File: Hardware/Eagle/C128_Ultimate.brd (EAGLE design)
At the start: 62.2 x 83.2 mm, 5 parts, among them IC1 0RB_COMMODORE_EXPANSION_PORT_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, X4 TSW-122-07-G-Q

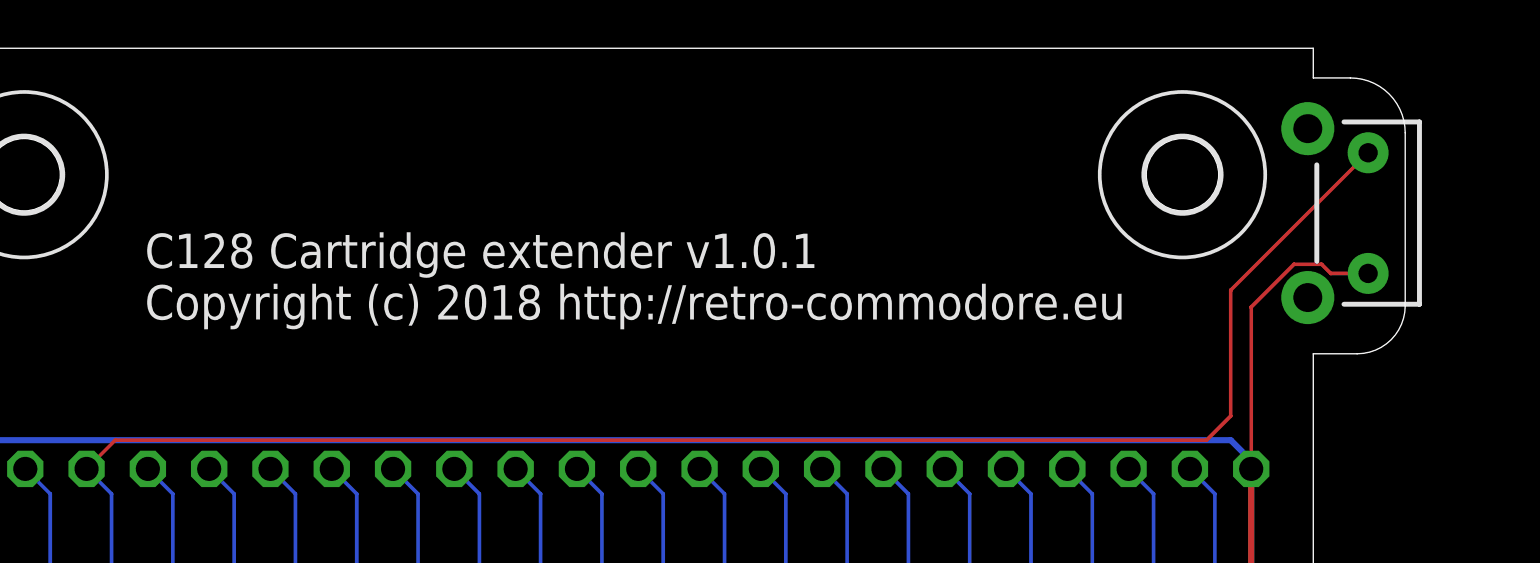
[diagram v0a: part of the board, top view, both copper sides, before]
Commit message: Update Hardware/Eagle/C128_Ultimate.brd
Properly moved reset button to bottom side
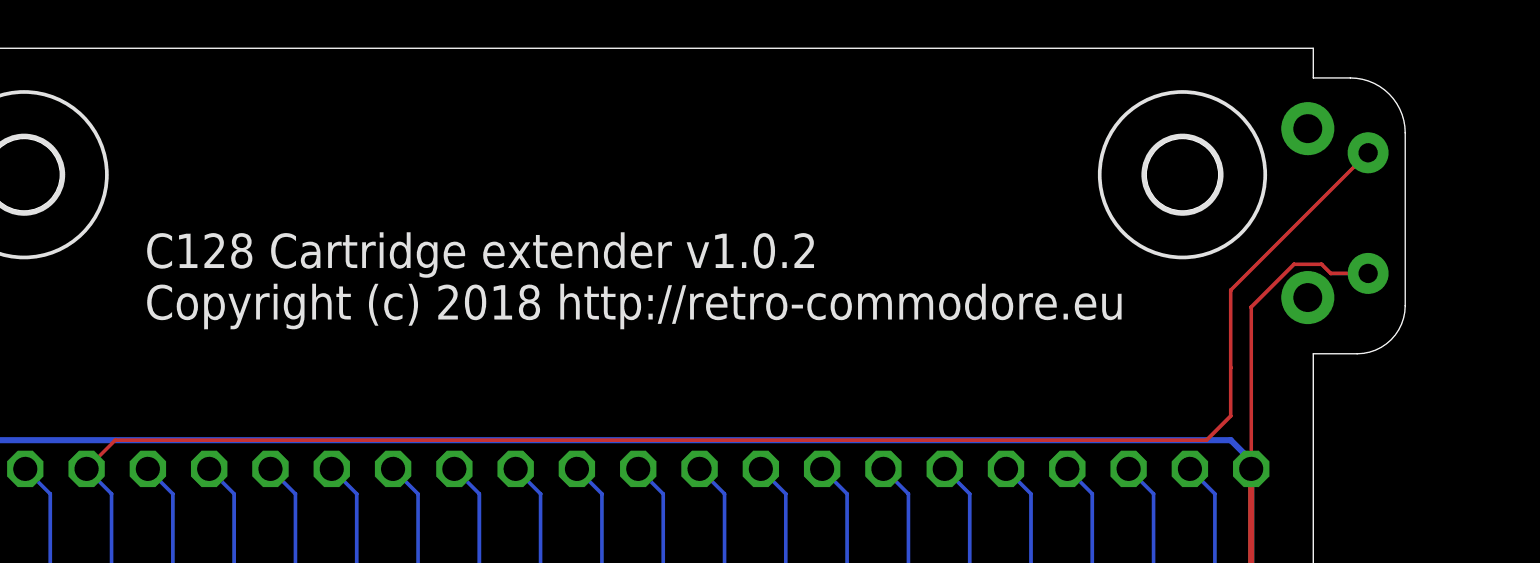
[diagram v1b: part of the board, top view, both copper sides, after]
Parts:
- flipped S1 to the bottom, turned to 270 degrees
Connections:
- net !RES: now also S1.1; no longer S1.2
- net GND: now also S1.2; no longer S1.1
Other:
- board text added: "C128 Cartridge extender v1.0.2 Copyright (c) 2018 http://retro-commodore.eu"
- board text removed: "C128 Cartridge extender v1.0.1 Copyright (c) 2018 http://retro-commodore.eu"
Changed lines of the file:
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@@
 <layers>
 <layer number="1" name="Top" color="4" fill="1" visible="yes" active="yes"/>
-<layer number="16" name="Bottom" color="1" fill="1" visible="yes" active="yes"/>
+<layer number="16" name="Bottom" color="1" fill="1" visible="no" active="yes"/>
 <layer number="17" name="Pads" color="2" fill="1" visible="yes" active="yes"/>
 <layer number="18" name="Vias" color="2" fill="1" visible="yes" active="yes"/>
@@
 <layer number="20" name="Dimension" color="24" fill="1" visible="yes" active="yes"/>
 <layer number="21" name="tPlace" color="7" fill="1" visible="yes" active="yes"/>
-<layer number="22" name="bPlace" color="7" fill="1" visible="yes" active="yes"/>
+<layer number="22" name="bPlace" color="7" fill="1" visible="no" active="yes"/>
 <layer number="23" name="tOrigins" color="15" fill="1" visible="yes" active="yes"/>
-<layer number="24" name="bOrigins" color="15" fill="1" visible="yes" active="yes"/>
+<layer number="24" name="bOrigins" color="15" fill="1" visible="no" active="yes"/>
 <layer number="25" name="tNames" color="7" fill="1" visible="yes" active="yes"/>
-<layer number="26" name="bNames" color="7" fill="1" visible="yes" active="yes"/>
+<layer number="26" name="bNames" color="7" fill="1" visible="no" active="yes"/>
 <layer number="27" name="tValues" color="7" fill="1" visible="no" active="yes"/>
 <layer number="28" name="bValues" color="7" fill="1" visible="no" active="yes"/>
@@
 <layer number="38" name="bTest" color="7" fill="1" visible="no" active="yes"/>
 <layer number="39" name="tKeepout" color="4" fill="11" visible="yes" active="yes"/>
-<layer number="40" name="bKeepout" color="1" fill="11" visible="yes" active="yes"/>
+<layer number="40" name="bKeepout" color="1" fill="11" visible="no" active="yes"/>
 <layer number="41" name="tRestrict" color="4" fill="10" visible="yes" active="yes"/>
-<layer number="42" name="bRestrict" color="1" fill="10" visible="yes" active="yes"/>
+<layer number="42" name="bRestrict" color="1" fill="10" visible="no" active="yes"/>
 <layer number="43" name="vRestrict" color="2" fill="10" visible="no" active="yes"/>
 <layer number="44" name="Drills" color="7" fill="1" visible="no" active="yes"/>
@@
 <layer number="50" name="dxf" color="7" fill="1" visible="no" active="no"/>
 <layer number="51" name="tDocu" color="7" fill="1" visible="yes" active="yes"/>
-<layer number="52" name="bDocu" color="7" fill="1" visible="yes" active="yes"/>
+<layer number="52" name="bDocu" color="7" fill="1" visible="no" active="yes"/>
 <layer number="53" name="tGND_GNDA" color="7" fill="9" visible="no" active="no"/>
 <layer number="54" name="bGND_GNDA" color="1" fill="9" visible="no" active="no"/>
@@
 <wire x1="0" y1="9.9314" x2="0.5334" y2="9.398" width="0" layer="20" curve="90"/>
 <wire x1="0.5334" y1="9.398" x2="0.635" y2="9.2964" width="0" layer="20" curve="-90"/>
-<text x="10" y="72" size="1.4224" layer="25">C128 Cartridge extender v1.0.1
+<text x="10" y="72" size="1.4224" layer="25">C128 Cartridge extender v1.0.2
 Copyright (c) 2018 http://retro-commodore.eu</text>
 </plain>
@@
 <elements>
 <element name="IC1" library="C64CartridgeEdgeConnector" package="0RB_COMMODORE_MA100-22-2" value="0RB_COMMODORE_EXPANSION_PORT_C64" x="29.21" y="5.08" smashed="yes"/>
-<element name="S1" library="SparkFun-Switches" library_urn="urn:adsk.eagle:library:535" package="TACTILE_SWITCH_PTH_RIGHT_ANGLE_KIT" package3d_urn="urn:adsk.eagle:package:40168/1" value="MOMENTARY-SWITCH-SPST-PTH-RIGHT-ANGLE-KIT" x="60.6933" y="76.4093" smashed="yes" rot="R90">
-<attribute name="PROD_ID" value="CONN-10672" x="60.6933" y="76.4093" size="1.778" layer="27" rot="R90" display="off"/>
-<attribute name="SF_SKU" value="COM-10791" x="60.6933" y="76.4093" size="1.778" layer="27" rot="R90" display="off"/>
+<element name="S1" library="SparkFun-Switches" library_urn="urn:adsk.eagle:library:535" package="TACTILE_SWITCH_PTH_RIGHT_ANGLE_KIT" package3d_urn="urn:adsk.eagle:package:40168/1" value="MOMENTARY-SWITCH-SPST-PTH-RIGHT-ANGLE-KIT" x="60.6933" y="76.4093" smashed="yes" rot="MR270">
+<attribute name="PROD_ID" value="CONN-10672" x="60.6933" y="76.4093" size="1.778" layer="28" rot="MR270" display="off"/>
+<attribute name="SF_SKU" value="COM-10791" x="60.6933" y="76.4093" size="1.778" layer="28" rot="MR270" display="off"/>
 </element>
 <element name="X4" library="con-samtec" package="TSW-122-XX-G-Q" value="TSW-122-07-G-Q" x="29.1778" y="63.2696" smashed="yes" rot="R180">
@@
 <contactref element="IC1" pad="A"/>
 <contactref element="IC1" pad="Z"/>
-<contactref element="S1" pad="1"/>
 <wire x1="2.54" y1="4.7752" x2="2.54" y2="60" width="0.254" layer="1"/>
 <contactref element="X4" pad="1"/>
@@
 <wire x1="55.8478" y1="4.8074" x2="55.88" y2="4.7752" width="0.1524" layer="1"/>
 <wire x1="58.7654125" y1="74.2905" x2="57.6211875" y2="74.2905" width="0.1524" layer="1"/>
-<wire x1="60.6933" y1="73.9093" x2="59.1466125" y2="73.9093" width="0.1524" layer="1"/>
-<wire x1="59.1466125" y1="73.9093" x2="58.7654125" y2="74.2905" width="0.1524" layer="1"/>
+<wire x1="58.7654125" y1="74.2905" x2="59.1466125" y2="73.9093" width="0.1524" layer="1"/>
 <wire x1="57.6211875" y1="74.2905" x2="55.8478" y2="72.5171125" width="0.1524" layer="1"/>
 <wire x1="55.8478" y1="72.5171125" x2="55.8478" y2="65.8096" width="0.1524" layer="1"/>
@@
 <wire x1="55" y1="67" x2="3.6982" y2="67" width="0.254" layer="16"/>
 <wire x1="3.6982" y1="67" x2="2.5078" y2="65.8096" width="0.254" layer="16"/>
+<contactref element="S1" pad="2"/>
+<wire x1="59.1466125" y1="73.9093" x2="60.6933" y2="73.9093" width="0.1524" layer="1"/>
 <wire x1="55.8478" y1="65.8096" x2="55.8478" y2="60.7296" width="0" layer="19" extent="1-1"/>
 <wire x1="2.5078" y1="60.7296" x2="2.54" y2="60.6974" width="0" layer="19" extent="1-1"/>
@@
 <signal name="!RES">
 <contactref element="IC1" pad="C"/>
-<contactref element="S1" pad="2"/>
 <contactref element="X4" pad="5"/>
-<wire x1="55" y1="73.216" x2="60.6933" y2="78.9093" width="0.1524" layer="1"/>
 <wire x1="7.62" y1="4.7752" x2="7.62" y2="59.2978" width="0.1524" layer="16"/>
 <wire x1="7.62" y1="59.2978" x2="8.623" y2="60.3008" width="0.1524" layer="16"/>
@@
 <wire x1="7.5878" y1="65.8096" x2="8.7782" y2="67" width="0.1524" layer="1"/>
 <wire x1="54" y1="67" x2="55" y2="68" width="0.1524" layer="1"/>
-<wire x1="55" y1="68" x2="55" y2="73.216" width="0.1524" layer="1"/>
+<wire x1="55" y1="68" x2="55" y2="70" width="0.1524" layer="1"/>
 <wire x1="8.7782" y1="67" x2="54" y2="67" width="0.1524" layer="1"/>
+<contactref element="S1" pad="1"/>
+<wire x1="55" y1="70" x2="55" y2="73.216" width="0.1524" layer="1"/>
+<wire x1="55" y1="73.216" x2="60.6933" y2="78.9093" width="0.1524" layer="1"/>
 </signal>
 <signal name="!DMA">
